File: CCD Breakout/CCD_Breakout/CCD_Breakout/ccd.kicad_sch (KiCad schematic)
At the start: 2 parts

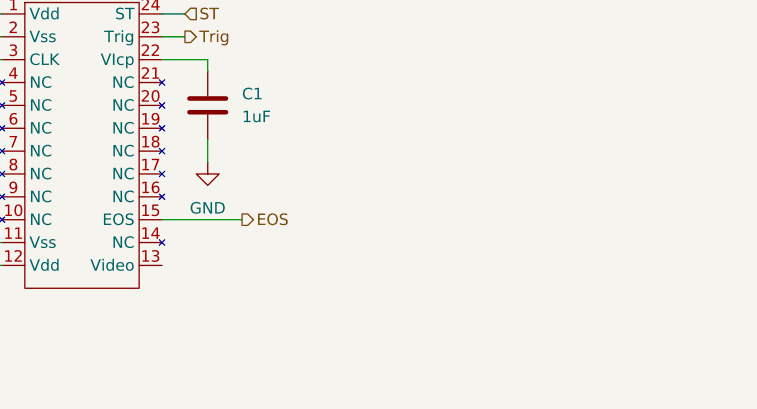
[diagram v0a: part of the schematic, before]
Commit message: Omp amp added
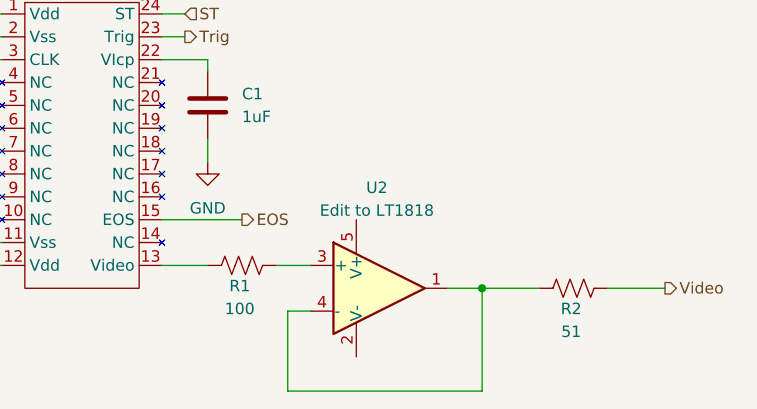
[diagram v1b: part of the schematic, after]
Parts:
- added R1: 100, symbol Device:R_US
- added R2: 51, symbol Device:R_US
- added U2: Edit to LT1818, Package_TO_SOT_SMD:TSOT-23-5, symbol Amplifier_Operational:OPA188xxDBV
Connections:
- net at U1.13 (Video): now also R1.2
- new net: R2.2, U2.1, U2.4 (-)
- new net: R1.1, U2.3 (+)
- new net Video: R2.1

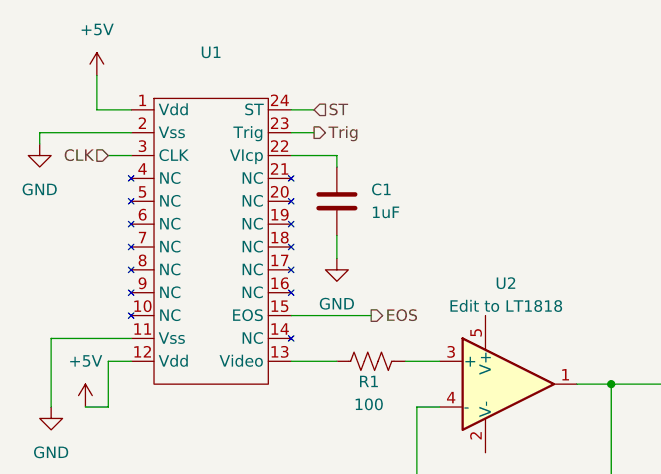
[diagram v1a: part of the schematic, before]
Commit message: Added Missing Resistors to CCD
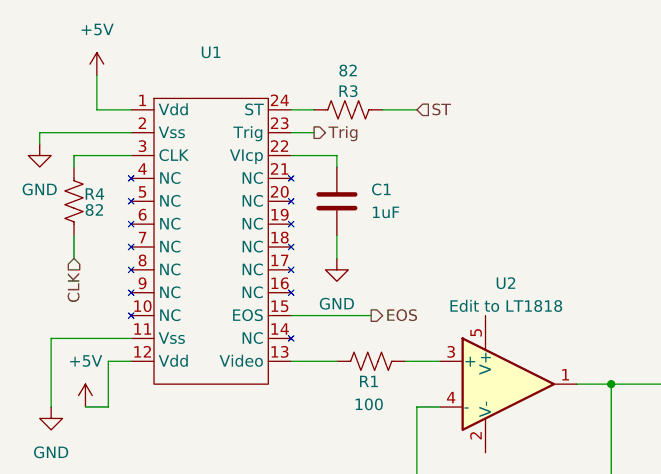
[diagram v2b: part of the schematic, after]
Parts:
- added R3, R4: 82, symbol Device:R_US
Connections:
- net CLK: now also R4.2; no longer U1.3 (CLK)
- net ST: now also R3.1; no longer U1.24 (ST)
- new net: R4.1, U1.3 (CLK)
- new net: R3.2, U1.24 (ST)
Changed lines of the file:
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@@
+	(wire
+		(pts
+			(xy 193.04 135.89) (xy 171.45 135.89)
+		)
+		(stroke
+			(width 0)
+			(type default)
+		)
+	)
+	(wire
+		(pts
+			(xy 157.48 116.84) (xy 166.37 116.84)
+		)
+		(stroke
+			(width 0)
+			(type default)
+		)
+	)
+	(wire
+		(pts
+			(xy 170.18 121.92) (xy 173.99 121.92)
+		)
+		(stroke
+			(width 0)
+			(type default)
+		)
+	)
+	(wire
+		(pts
+			(xy 129.54 96.52) (xy 139.7 96.52)
+		)
+		(stroke
+			(width 0)
+			(type default)
+		)
+	)
+	(wire
+		(pts
+			(xy 133.35 100.33) (xy 133.35 99.06)
+		)
+		(stroke
+			(width 0)
+			(type default)
+		)
+	)
+	(wire
+		(pts
+			(xy 133.35 99.06) (xy 139.7 99.06)
+		)
+		(stroke
+			(width 0)
+			(type default)
+		)
+	)
+	(wire
+		(pts
+			(xy 133.35 107.95) (xy 133.35 110.49)
+		)
+		(stroke
+			(width 0)
+			(type default)
+		)
+	)
+	(wire
+		(pts
+			(xy 129.54 97.79) (xy 129.54 96.52)
+		)
+		(stroke
+			(width 0)
+			(type default)
+		)
+	)
+	(wire
+		(pts
+			(xy 134.62 127) (xy 137.16 127)
+		)
+		(stroke
+			(width 0)
+			(type default)
+		)
+	)
 	(wire
 		(pts
@@
 	(wire
 		(pts
-			(xy 193.04 135.89) (xy 171.45 135.89)
-		)
-		(stroke
-			(width 0)
-			(type default)
-		)
-	)
-	(wire
-		(pts
-			(xy 157.48 116.84) (xy 166.37 116.84)
-		)
-		(stroke
-			(width 0)
-			(type default)
-		)
-	)
-	(wire
-		(pts
-			(xy 170.18 121.92) (xy 173.99 121.92)
-		)
-		(stroke
-			(width 0)
-			(type default)
-		)
-	)
-	(wire
-		(pts
-			(xy 129.54 96.52) (xy 139.7 96.52)
-		)
-		(stroke
-			(width 0)
-			(type default)
-		)
-	)
-	(wire
-		(pts
-			(xy 137.16 99.06) (xy 139.7 99.06)
-		)
-		(stroke
-			(width 0)
-			(type default)
-		)
-	)
-	(wire
-		(pts
-			(xy 129.54 97.79) (xy 129.54 96.52)
-		)
-		(stroke
-			(width 0)
-			(type default)
-		)
-	)
-	(wire
-		(pts
-			(xy 134.62 127) (xy 137.16 127)
-		)
-		(stroke
-			(width 0)
-			(type default)
-		)
-	)
-	(wire
-		(pts
 			(xy 162.56 99.06) (xy 157.48 99.06)
 		)
@@
 		(pts
 			(xy 171.45 127) (xy 173.99 127)
+		)
+		(stroke
+			(width 0)
+			(type default)
+		)
+	)
+	(wire
+		(pts
+			(xy 167.64 93.98) (xy 171.45 93.98)
 		)
 		(stroke
@@
 	(hierarchical_label "CLK"
 		(shape input)
-		(at 137.16 99.06 180)
+		(at 133.35 110.49 270)
 		(effects
 			(font
@@
 	(hierarchical_label "ST"
 		(shape input)
-		(at 160.02 93.98 0)
+		(at 171.45 93.98 0)
 		(effects
 			(font
@@
 			)
 			(justify left)
+		)
+	)
+	(symbol
+		(lib_id "Device:R_US")
+		(at 133.35 104.14 0)
+		(unit 1)
+		(exclude_from_sim no)
+		(in_bom yes)
+		(on_board yes)
+		(dnp no)
+		(property "Reference" "R4"
+			(at 135.636 103.378 0)
+			(effects
+				(font
+					(size 1.27 1.27)
+				)
+			)
+		)
+		(property "Value" "82"
+			(at 135.636 105.156 0)
+			(effects
+				(font
+					(size 1.27 1.27)
+				)
+			)
+		)
+		(property "Footprint" ""
+			(at 134.366 104.394 90)
+			(effects
+				(font
+					(size 1.27 1.27)
+				)
+				(hide yes)
+			)
+		)
+		(property "Datasheet" "~"
+			(at 133.35 104.14 0)
+			(effects
+				(font
+					(size 1.27 1.27)
+				)
+				(hide yes)
+			)
+		)
+		(property "Description" "Resistor, US symbol"
+			(at 133.35 104.14 0)
+			(effects
+				(font
+					(size 1.27 1.27)
+				)
+				(hide yes)
+			)
+		)
+		(pin "1"
+		)
+		(pin "2"
+		)
+		(instances
+			(project "CCD_Breakout"
+				(path "/102965ac-29c6-4f96-94a4-d07431f6d693/df02ed66-bf6d-4cf2-9207-d6cfc3fa7e76"
+					(reference "R4")
+					(unit 1)
+				)
+			)
 		)
 	)
@@
 					(unit 1)
 				)
+			)
+		)
+	)
+	(symbol
+		(lib_id "Device:R_US")
+		(at 163.83 93.98 270)
+		(unit 1)
+		(exclude_from_sim no)
+		(in_bom yes)
+		(on_board yes)
+		(dnp no)
+		(property "Reference" "R3"
+			(at 163.83 91.948 90)
+			(effects
+				(font
+					(size 1.27 1.27)
+				)
+			)
+		)
+		(property "Value" "82"
+			(at 163.83 89.662 90)
+			(effects
+				(font
+					(size 1.27 1.27)
+				)
+			)
+		)
+		(property "Footprint" ""
+			(at 163.576 94.996 90)
+			(effects
+				(font
+					(size 1.27 1.27)
+				)
+				(hide yes)
+			)
+		)
+		(property "Datasheet" "~"
+			(at 163.83 93.98 0)
+			(effects
+				(font
+					(size 1.27 1.27)
+				)
+				(hide yes)
+			)
+		)
+		(property "Description" "Resistor, US symbol"
+			(at 163.83 93.98 0)
+			(effects
+				(font
+					(size 1.27 1.27)
+				)
+				(hide yes)
+			)
+		)
+		(pin "1"
+		)
+		(pin "2"
+		)
+		(instances
+			(project "CCD_Breakout"
+				(path "/102965ac-29c6-4f96-94a4-d07431f6d693/df02ed66-bf6d-4cf2-9207-d6cfc3fa7e76"
+					(reference "R3")
+					(unit 1)
+				)

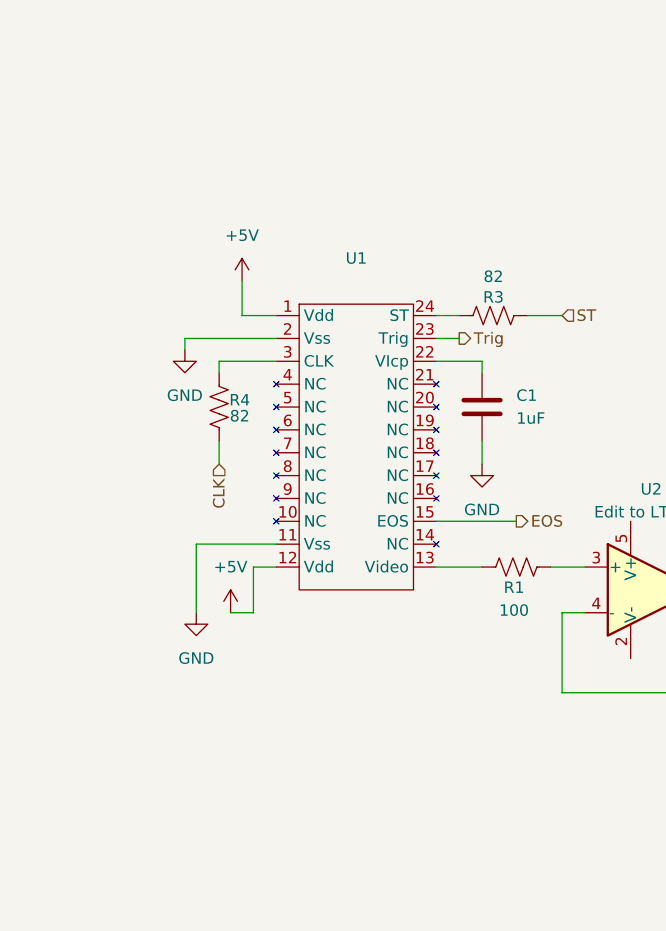
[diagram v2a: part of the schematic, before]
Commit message: Adding Decouplers
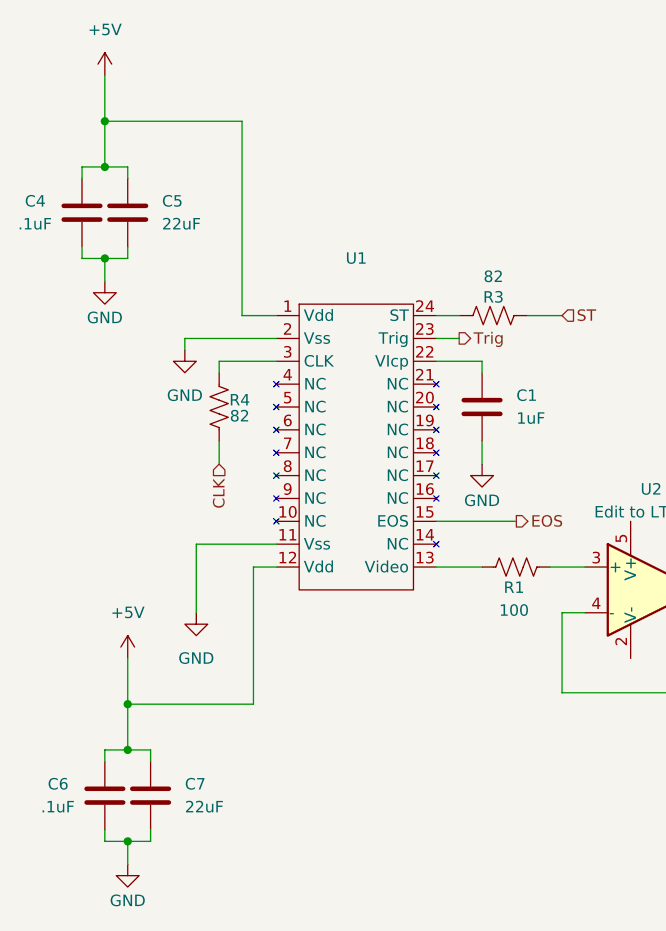
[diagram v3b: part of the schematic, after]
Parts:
- added C4, C6: .1uF, symbol Device:C
- added C5, C7: 22uF, symbol Device:C
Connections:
- net +5V: now also C4.1, C5.1, C6.1, C7.1
- net GND: now also C4.2, C5.2, C6.2, C7.2

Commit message: Honestly a bunch of rapid changes
CCD ADC
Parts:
- removed R2: 51, symbol Device:R_US
- removed U2: Edit to LT1818, Package_TO_SOT_SMD:TSOT-23-5, symbol Amplifier_Operational:OPA188xxDBV
- added C8: .1uF, symbol Device:C
- added C9: 22uF, symbol Device:C
- added R8: 51, symbol Device:R_US
- added U4: OPA322AIDBVR, DBV5, symbol 2025-10-09_01-55-37:OPA322AIDBVR
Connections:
- net +5V: now also C8.1, C9.1, U4.5 (V+)
- net GND: now also C8.2, C9.2, U4.2 (V-)
- net Video: now also R8.1
- net at R1.1: now also U4.3 (IN+)
- new net: R8.2, U4.1 (OUT), U4.4 (IN-)

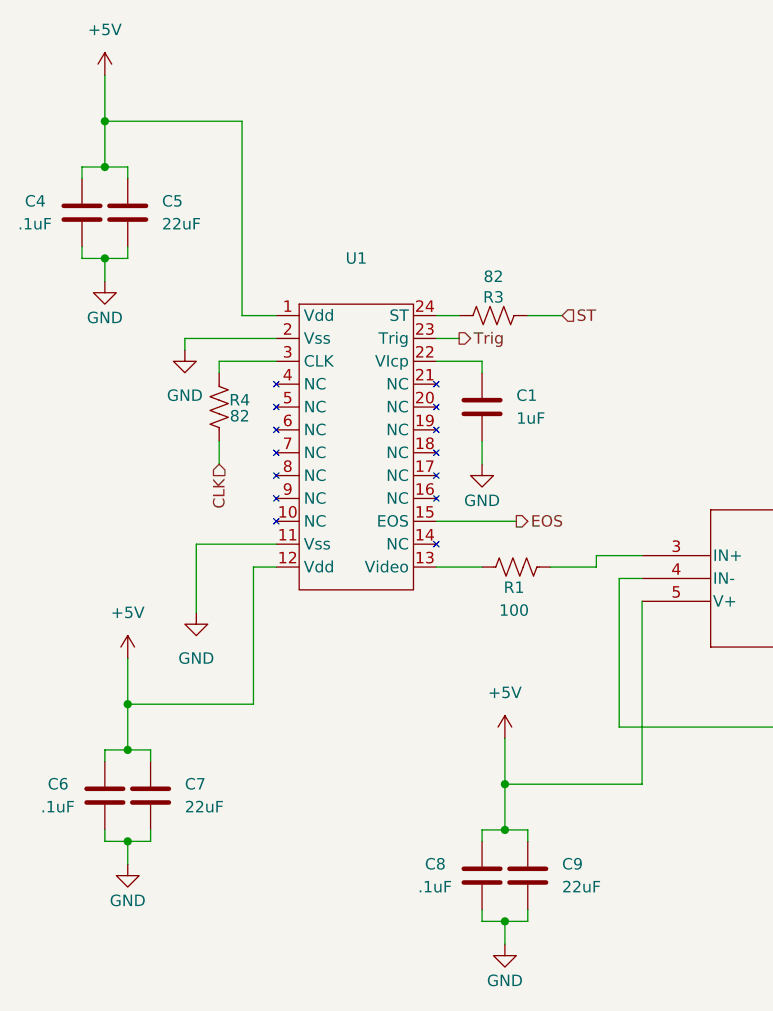
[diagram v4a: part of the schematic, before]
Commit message: Removed Unnecessary Filtering Capacitors
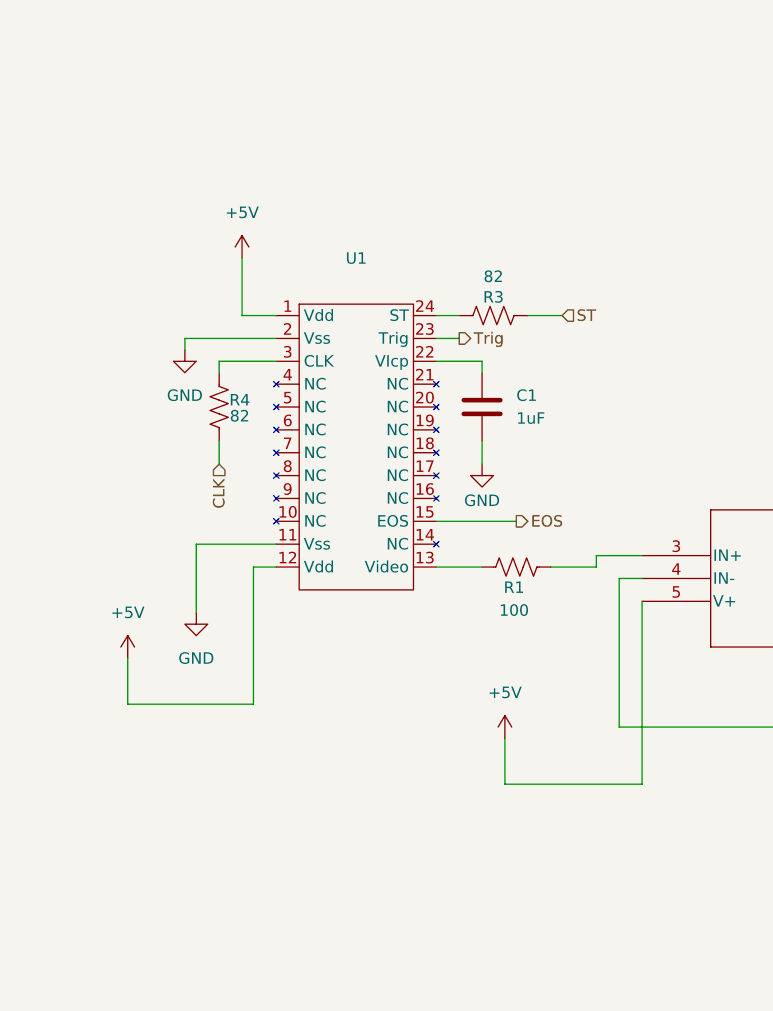
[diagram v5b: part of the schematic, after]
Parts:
- removed C4, C6, C8: .1uF, symbol Device:C
- removed C5, C7, C9: 22uF, symbol Device:C

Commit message: Possible Buffer Design
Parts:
- added U2: SN74LV125APWR, PW14, symbol 2025-10-10_03-36-18:SN74LV125APWR
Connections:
- net +5V: now also U2.14 (VCC)
- net CLK: now also U2.5 (2A); no longer R4.2
- net EOS: now also U2.8 (3Y); no longer U1.15 (EOS)
- net GND: now also U2.1 (*1OE), U2.10 (*3OE), U2.13 (*4OE), U2.4 (*2OE), U2.7 (GND)
- net ST: now also U2.2 (1A); no longer R3.1
- net Trig: now also U2.11 (4Y); no longer U1.23 (Trig)
- new net CLKb: R4.2, U2.6 (2Y)
- new net EOSb: U1.15 (EOS), U2.9 (3A)
- new net STb: R3.1, U2.3 (1Y)
- new net Trigb: U1.23 (Trig), U2.12 (4A)

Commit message: ADC 1.8 Pin
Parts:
- removed U2: SN74LV125APWR, PW14, symbol 2025-10-10_03-36-18:SN74LV125APWR
- added U5: 74HC541PW_118, TSSOP20_SOT360-1_NEX, symbol 2025-10-14_22-52-15:74HC541PW_118
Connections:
- net +5V: now also U5.20 (VCC)
- net CLK: now also U5.3 (A1)
- net CLKb: now also U5.17 (Y1)
- net EOS: now also U5.15 (Y3)
- net EOSb: now also U5.5 (A3)
- net GND: now also U5.1 (OE1), U5.10 (GND), U5.11 (Y7), U5.12 (Y6), U5.13 (Y5), U5.14 (Y4), U5.19 (OE2), U5.6 (A4), U5.7 (A5), U5.8 (A6), U5.9 (A7)
- net ST: now also U5.2 (A0)
- net STb: now also U5.18 (Y0)
- net Trig: now also U5.16 (Y2)
- net Trigb: now also U5.4 (A2)

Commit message: OpAmp IC
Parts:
- removed U4: OPA322AIDBVR, DBV5, symbol 2025-10-09_01-55-37:OPA322AIDBVR
- added C7: 20uF, symbol Device:C_US
- added R10, R11, R6: R_US, symbol Device:R_US
- added R12: 2000, symbol Device:R_US
- added R13: 3000, symbol Device:R_US
- added R5, R9: 10000, symbol Device:R_US
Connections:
- net +5V: now also R5.1
- net GND: now also C7.2, R10.2, R11.2, R6.2, R9.1
- net Video: now also R13.1; no longer R8.1
- net opINA+: now reaches R1.1
- net opINA-: now reaches R8.2
- new net Videob: R8.1
- new net opINB+: C7.1, R10.1, R11.1, R5.2, R6.1, R9.2
- new net opINB-: R12.2
- new net opINC-: R12.1, R13.2
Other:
- moved on the sheet: C1, R1, R3, R4, R8, U1, U5
